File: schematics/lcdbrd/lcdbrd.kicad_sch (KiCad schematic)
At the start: 11 parts, among them J1 Conn_02x32_Odd_Even, J2 Conn_02x20_Odd_Even

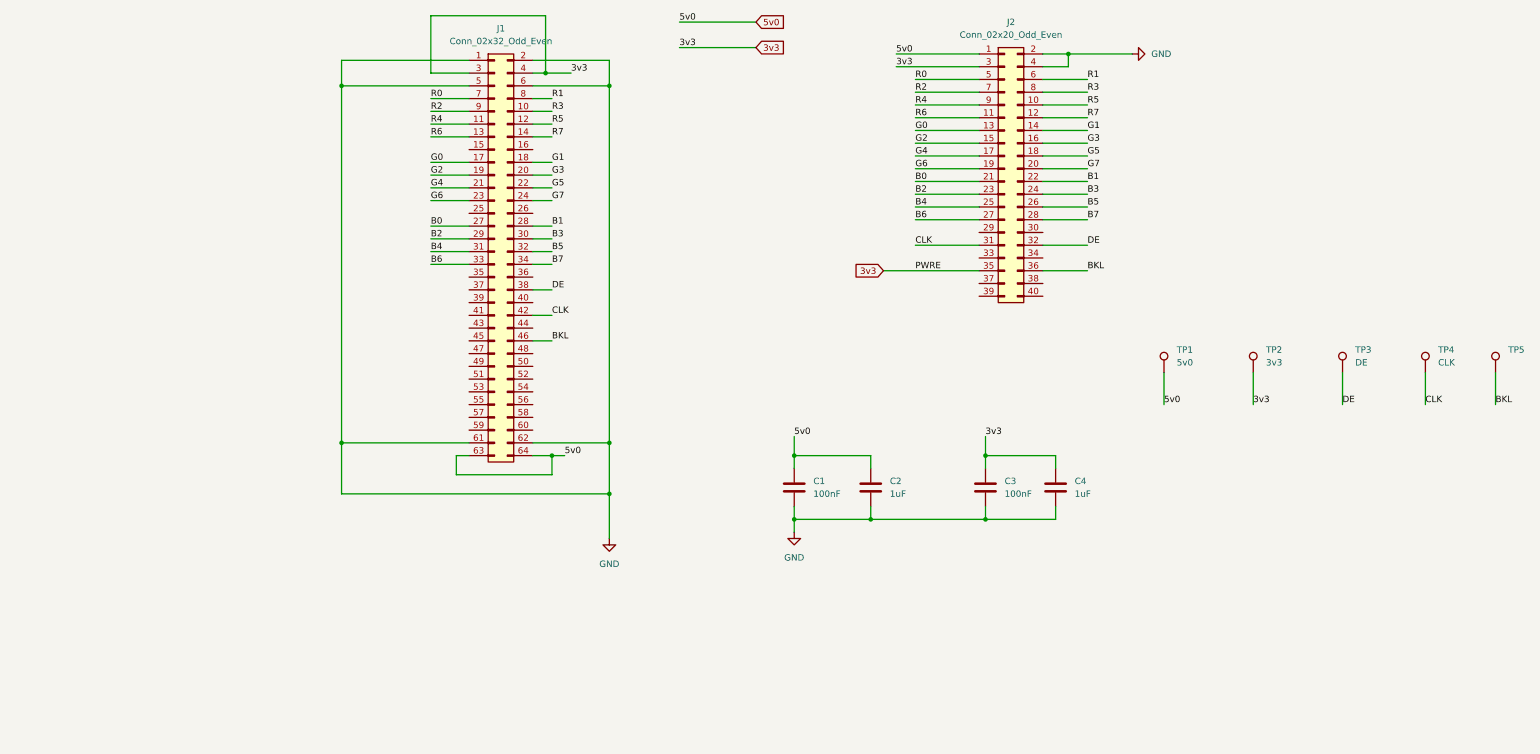
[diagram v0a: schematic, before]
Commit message: Rv32: Added some legend to LCD board schematics.
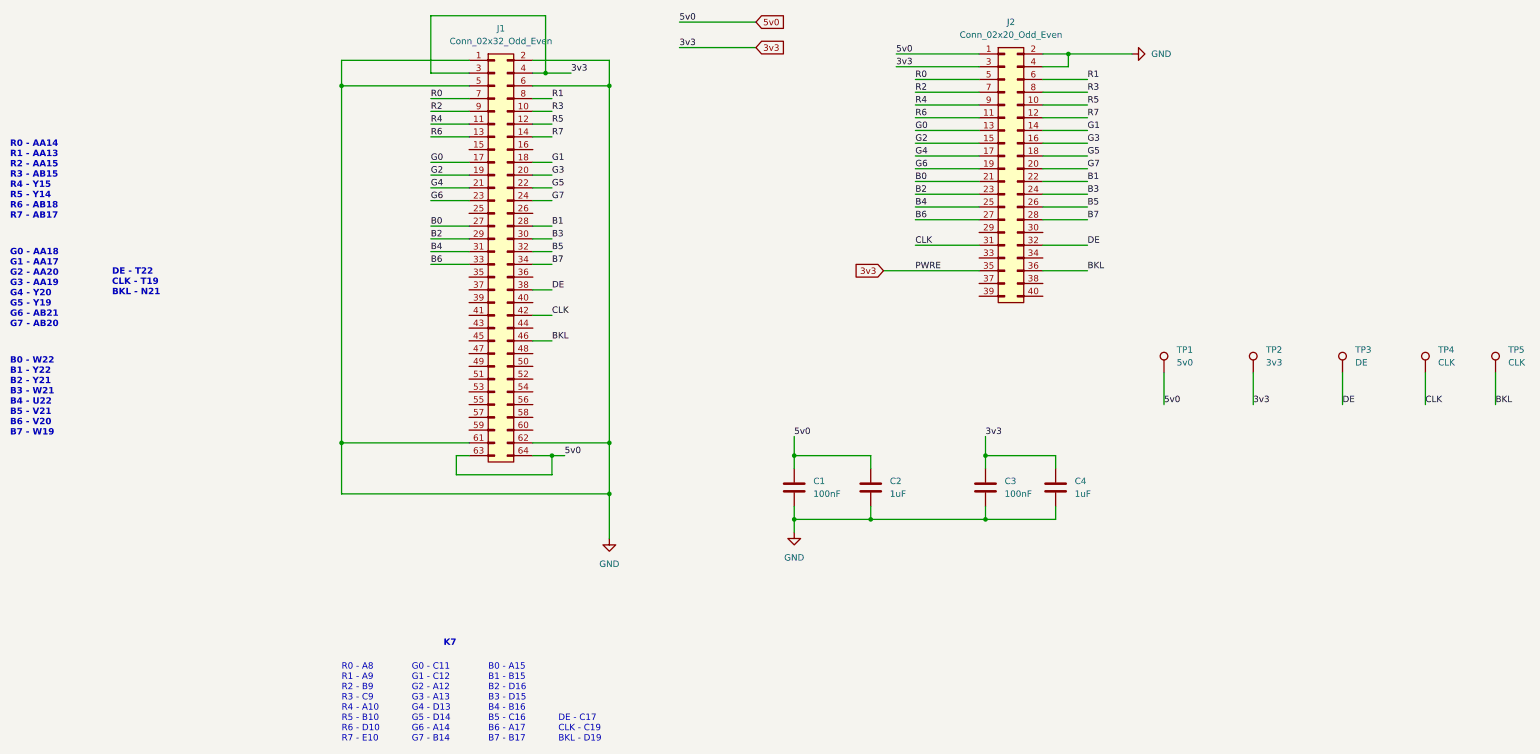
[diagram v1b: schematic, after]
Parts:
- TP5: value (none) -> CLK; footprint (none) -> TestPoint:TestPoint_Pad_D1.5mm
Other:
- note added: "B0 - A15 B1 - B15 B2 - D16 B3 - D15 B4 - B16 B5 - C16 B6 - A17 B7 - B17"
- note added: "B0 - W22 B1 - Y22 B2 - Y21 B3 - W21 B4 - U22 B5 - V21 B6 - V20 B7 - W19"
- note added: "DE - C17 CLK - C19 BKL - D19"
- note added: "DE - T22 CLK - T19 BKL - N21"
- note added: "G0 - AA18 G1 - AA17 G2 - AA20 G3 - AA19 G4 - Y20 G5 - Y19 G6 - AB21 G7 - AB20"
- note added: "G0 - C11 G1 - C12 G2 - A12 G3 - A13 G4 - D13 G5 - D14 G6 - A14 G7 - B14"
- note added: "K7"
- note added: "R0 - A8 R1 - A9 R2 - B9 R3 - C9 R4 - A10 R5 - B10 R6 - D10 R7 - E10"
- note added: "R0 - AA14 R1 - AA13 R2 - AA15 R3 - AB15 R4 - Y15 R5 - Y14 R6 - AB18 R7 - AB17"
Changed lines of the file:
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@@
     (stroke (width 0) (type default) (color 0 0 0 0))
+  )
+  (text "B0 - W22\nB1 - Y22\nB2 - Y21\nB3 - W21\nB4 - U22\nB5 - V21\nB6 - V20\nB7 - W19"
+    (at -43.18 124.46 0)
+    (effects (font (size 1.27 1.27) bold) (justify left bottom))
+  )
+  (text "R0 - AA14\nR1 - AA13\nR2 - AA15\nR3 - AB15\nR4 - Y15\nR5 - Y14\nR6 - AB18\nR7 - AB17"
+    (at -43.18 81.28 0)
+    (effects (font (size 1.27 1.27) bold) (justify left bottom))
+  )
+  (text "DE - C17\nCLK - C19\nBKL - D19" (at 66.04 185.42 0)
+    (effects (font (size 1.27 1.27)) (justify left bottom))
+  )
+  (text "R0 - A8\nR1 - A9\nR2 - B9\nR3 - C9\nR4 - A10\nR5 - B10\nR6 - D10\nR7 - E10"
+    (at 22.86 185.42 0)
+    (effects (font (size 1.27 1.27)) (justify left bottom))
+  )
+  (text "G0 - C11\nG1 - C12\nG2 - A12\nG3 - A13\nG4 - D13\nG5 - D14\nG6 - A14\nG7 - B14"
+    (at 36.83 185.42 0)
+    (effects (font (size 1.27 1.27)) (justify left bottom))
+  )
+  (text "B0 - A15\nB1 - B15\nB2 - D16\nB3 - D15\nB4 - B16\nB5 - C16\nB6 - A17\nB7 - B17"
+    (at 52.07 185.42 0)
+    (effects (font (size 1.27 1.27)) (justify left bottom))
+  )
+  (text "DE - T22\nCLK - T19\nBKL - N21" (at -22.86 96.52 0)
+    (effects (font (size 1.27 1.27) bold) (justify left bottom))
+  )
+  (text "K7" (at 43.18 166.37 0)
+    (effects (font (size 1.27 1.27) (thickness 0.254) bold) (justify left bottom))
+  )
+  (text "G0 - AA18\nG1 - AA17\nG2 - AA20\nG3 - AA19\nG4 - Y20\nG5 - Y19\nG6 - AB21\nG7 - AB20"
+    (at -43.18 102.87 0)
+    (effects (font (size 1.27 1.27) bold) (justify left bottom))
   )
   (label "G0" (at 40.64 69.85 0)
@@
       (effects (font (size 1.27 1.27)) (justify left))
     )
-    (property "Value" "" (id 1) (at 255.27 109.7279 0)
-      (effects (font (size 1.27 1.27)) (justify left))
-    )
-    (property "Footprint" "" (id 2) (at 257.81 111.76 0)
-      (effects (font (size 1.27 1.27)) hide)
-    )
+    (property "Value" "CLK" (id 1) (at 255.27 109.7279 0)
+      (effects (font (size 1.27 1.27)) (justify left))
+    )
+    (property "Footprint" "TestPoint:TestPoint_Pad_D1.5mm" (id 2) (at 257.81 111.76 0)
+      (effects (font (size 1.27 1.27)) hide)
+    )

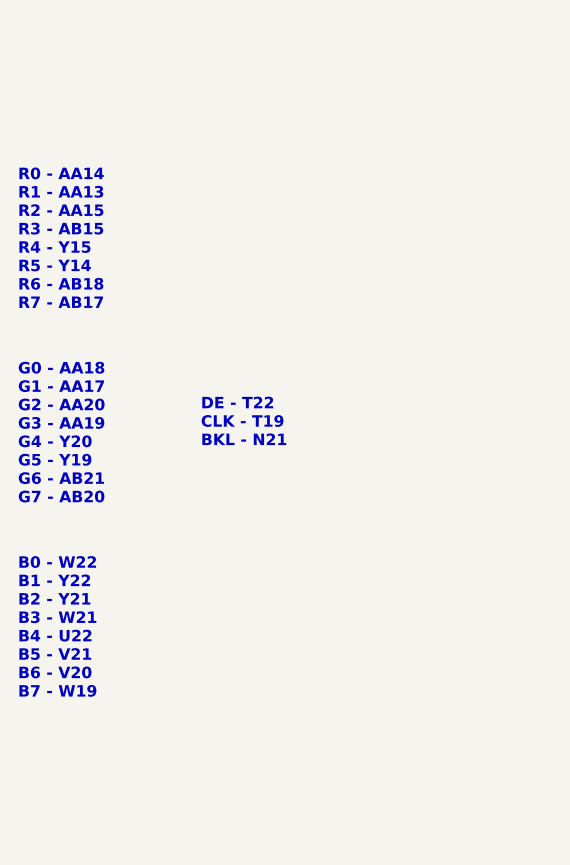
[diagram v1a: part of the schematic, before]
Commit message: Rv32: Updated SRAM brd schematic. Also updated legend in lcdbrd.
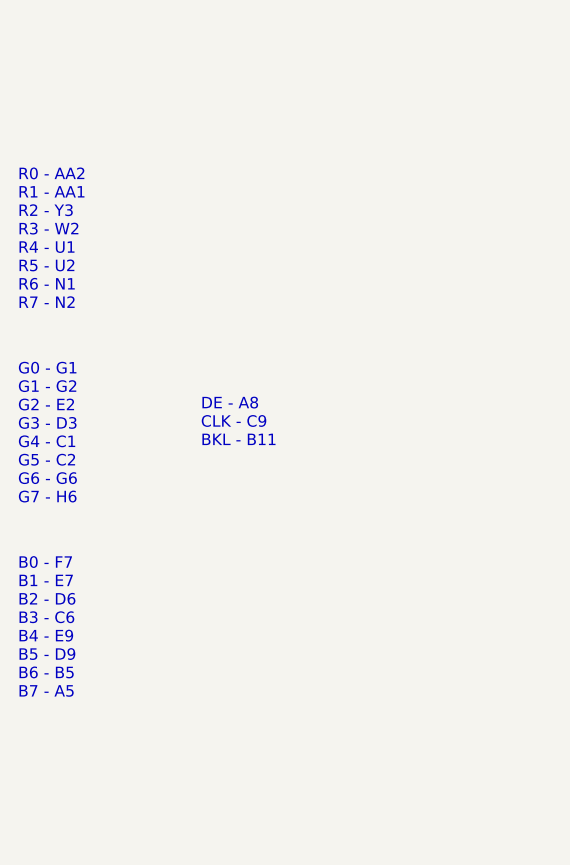
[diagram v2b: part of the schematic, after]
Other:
- note added: "B0 - F7 B1 - E7 B2 - D6 B3 - C6 B4 - E9 B5 - D9 B6 - B5 B7 - A5"
- note added: "DE - A8 CLK - C9 BKL - B11"
- note added: "G0 - G1 G1 - G2 G2 - E2 G3 - D3 G4 - C1 G5 - C2 G6 - G6 G7 - H6"
- note added: "R0 - AA2 R1 - AA1 R2 - Y3 R3 - W2 R4 - U1 R5 - U2 R6 - N1 R7 - N2"
- note removed: "B0 - W22 B1 - Y22 B2 - Y21 B3 - W21 B4 - U22 B5 - V21 B6 - V20 B7 - W19"
- note removed: "DE - T22 CLK - T19 BKL - N21"
- note removed: "G0 - AA18 G1 - AA17 G2 - AA20 G3 - AA19 G4 - Y20 G5 - Y19 G6 - AB21 G7 - AB20"
- note removed: "R0 - AA14 R1 - AA13 R2 - AA15 R3 - AB15 R4 - Y15 R5 - Y14 R6 - AB18 R7 - AB17"
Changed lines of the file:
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@@
     (stroke (width 0) (type default) (color 0 0 0 0))
   )
-  (text "B0 - W22\nB1 - Y22\nB2 - Y21\nB3 - W21\nB4 - U22\nB5 - V21\nB6 - V20\nB7 - W19"
+  (text "B0 - F7\nB1 - E7\nB2 - D6\nB3 - C6\nB4 - E9\nB5 - D9\nB6 - B5\nB7 - A5"
     (at -43.18 124.46 0)
-    (effects (font (size 1.27 1.27) bold) (justify left bottom))
+    (effects (font (size 1.27 1.27)) (justify left bottom))
   )
-  (text "R0 - AA14\nR1 - AA13\nR2 - AA15\nR3 - AB15\nR4 - Y15\nR5 - Y14\nR6 - AB18\nR7 - AB17"
+  (text "R0 - AA2\nR1 - AA1\nR2 - Y3\nR3 - W2\nR4 - U1\nR5 - U2\nR6 - N1\nR7 - N2"
     (at -43.18 81.28 0)
-    (effects (font (size 1.27 1.27) bold) (justify left bottom))
+    (effects (font (size 1.27 1.27)) (justify left bottom))
   )
   (text "DE - C17\nCLK - C19\nBKL - D19" (at 66.04 185.42 0)
@@
     (effects (font (size 1.27 1.27)) (justify left bottom))
   )
-  (text "DE - T22\nCLK - T19\nBKL - N21" (at -22.86 96.52 0)
-    (effects (font (size 1.27 1.27) bold) (justify left bottom))
+  (text "DE - A8\nCLK - C9\nBKL - B11" (at -22.86 96.52 0)
+    (effects (font (size 1.27 1.27)) (justify left bottom))
   )
   (text "K7" (at 43.18 166.37 0)
     (effects (font (size 1.27 1.27) (thickness 0.254) bold) (justify left bottom))
   )
-  (text "G0 - AA18\nG1 - AA17\nG2 - AA20\nG3 - AA19\nG4 - Y20\nG5 - Y19\nG6 - AB21\nG7 - AB20"
+  (text "G0 - G1\nG1 - G2\nG2 - E2\nG3 - D3\nG4 - C1\nG5 - C2\nG6 - G6\nG7 - H6"
     (at -43.18 102.87 0)
-    (effects (font (size 1.27 1.27) bold) (justify left bottom))
+    (effects (font (size 1.27 1.27)) (justify left bottom))
   )
   (label "G0" (at 40.64 69.85 0)
